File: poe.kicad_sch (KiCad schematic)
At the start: 59 parts, among them IC1 TPS2378DDA, J1 B2B-XH-A_LF__SN_, J6 SS-74800-144, U3 TPS2373-3RGW, U4 URB4805YMD-30WR3

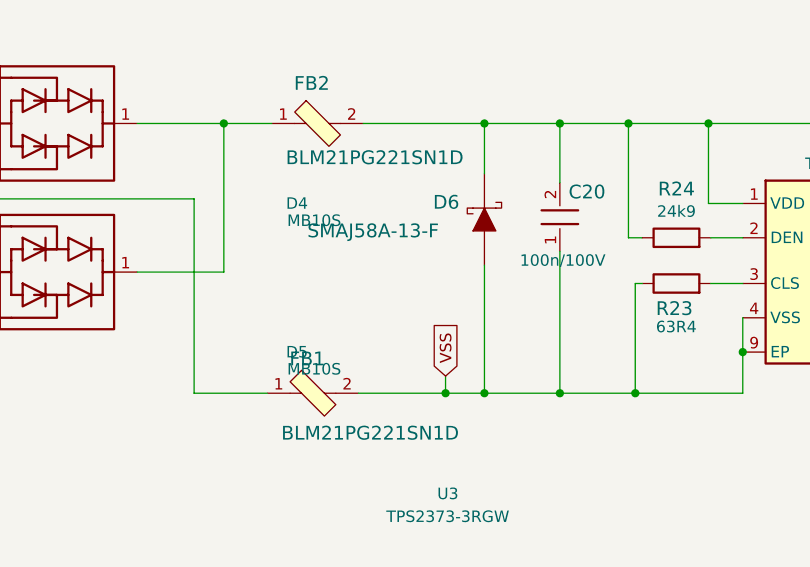
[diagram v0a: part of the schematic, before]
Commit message: Update D6 symbol and footprint
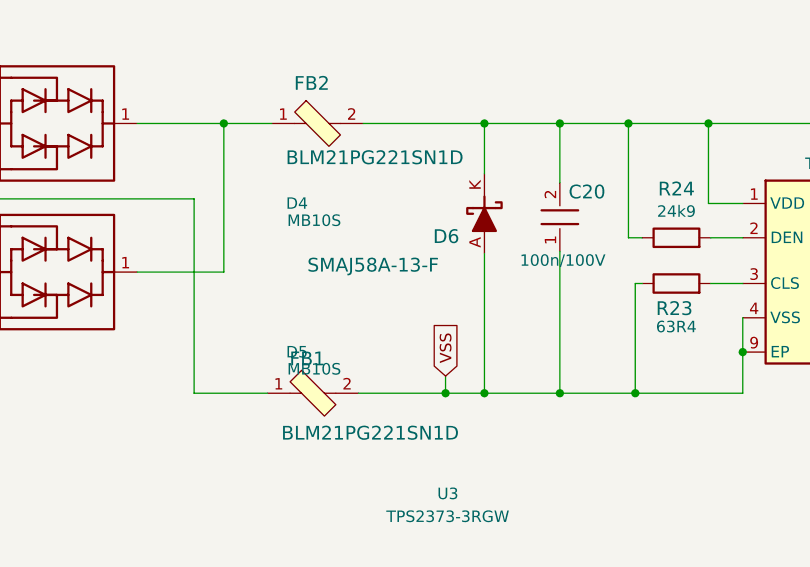
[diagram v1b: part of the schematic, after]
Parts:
- D6: footprint scalenode-cm4-baseboard-footprints:DO-214AC -> antmicro-footprints:DO-214AC; symbol scalenode-cm4-baseboard:SMAJ58A-13-F -> antmicroDiodesRectifiersSingle:SMAJ58A-13-F; Author (none) -> Antmicro; License (none) -> Apache-2.0
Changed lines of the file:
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@@
     (stroke (width 0) (type default) (color 0 0 0 0))
   )
-  (wire (pts (xy 109.982 165.608) (xy 109.982 179.832))
+  (wire (pts (xy 109.982 164.338) (xy 109.982 179.832))
     (stroke (width 0) (type default) (color 0 0 0 0))
   )
@@
     (pin "2")
   )
-  (symbol (lib_id "scalenode-cm4-baseboard:SMAJ58A-13-F") (at 109.982 160.528 90) (unit 1)
+  (symbol (lib_id "antmicroDiodesRectifiersSingle:SMAJ58A-13-F") (at 109.982 164.338 90) (unit 1)
     (in_bom yes) (on_board yes)
-    (property "Reference" "D6" (id 0) (at 104.267 158.623 90)
+    (property "Reference" "D6" (id 0) (at 104.267 162.433 90)
       (effects (font (size 1.524 1.524)) (justify right))
     )
-    (property "Value" "SMAJ58A-13-F" (id 1) (at 90.297 161.798 90)
+    (property "Value" "SMAJ58A-13-F" (id 1) (at 90.297 165.608 90)
       (effects (font (size 1.524 1.524)) (justify right))
     )
-    (property "Footprint" "scalenode-cm4-baseboard-footprints:DO-214AC" (id 2) (at 104.902 155.448 0)
-      (effects (font (size 1.524 1.524)) (justify left) hide)
+    (property "Footprint" "antmicro-footprints:DO-214AC" (id 2) (at 120.142 142.748 0)
+      (effects (font (size 1.27 1.27) (thickness 0.15)) (justify left bottom) hide)
     )
-    (property "Datasheet" "https://4donline.ihs.com/images/VipMasterIC/IC/DIOD/DIOD-S-A0001754755/DIOD-S-A0001754755-1.pdf?hkey=52A5661711E402568146F3353EA87419" (id 3) (at 102.362 155.448 0)
-      (effects (font (size 1.524 1.524)) (justify left) hide)
+    (property "Datasheet" "https://4donline.ihs.com/images/VipMasterIC/IC/DIOD/DIOD-S-A0001754755/DIOD-S-A0001754755-1.pdf?hkey=52A5661711E402568146F3353EA87419" (id 3) (at 122.682 142.748 0)
+      (effects (font (size 1.27 1.27) (thickness 0.15)) (justify left bottom) hide)
     )
-    (property "MPN" "SMAJ58A-13-F" (id 4) (at 97.282 155.448 0)
-      (effects (font (size 1.524 1.524)) (justify left) hide)
+    (property "MPN" "SMAJ58A-13-F" (id 4) (at 125.222 142.748 0)
+      (effects (font (size 1.27 1.27) (thickness 0.15)) (justify left bottom) hide)
     )
-    (property "Manufacturer" "Diodes Incorporated" (id 5) (at 82.042 155.448 0)
-      (effects (font (size 1.524 1.524)) (justify left) hide)
+    (property "Manufacturer" "Diodes Incorporated" (id 5) (at 127.762 142.748 0)
+      (effects (font (size 1.27 1.27) (thickness 0.15)) (justify left bottom) hide)
+    )
+    (property "Author" "Antmicro" (id 6) (at 130.302 142.748 0)
+      (effects (font (size 1.27 1.27) (thickness 0.15)) (justify left bottom) hide)
+    )
+    (property "License" "Apache-2.0" (id 7) (at 132.842 142.748 0)
+      (effects (font (size 1.27 1.27) (thickness 0.15)) (justify left bottom) hide)
     )
     (pin "A")

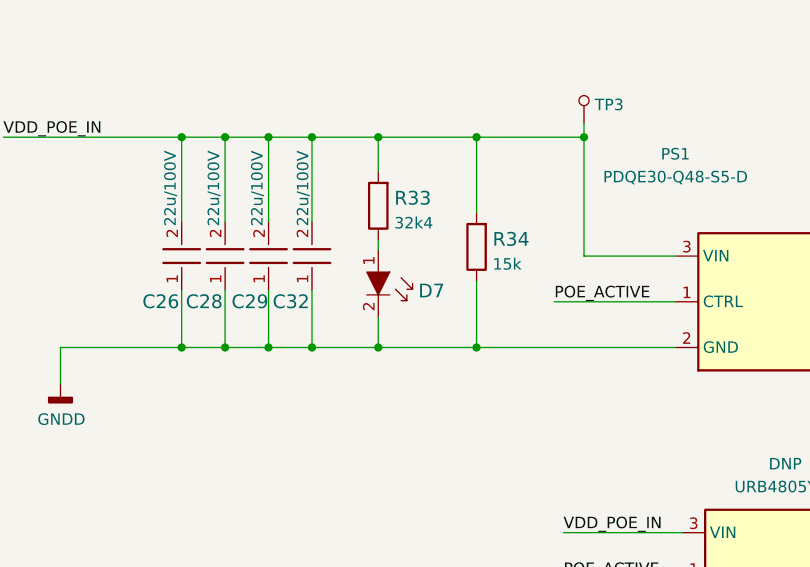
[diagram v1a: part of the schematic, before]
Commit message: Update D7 symbol and footprint
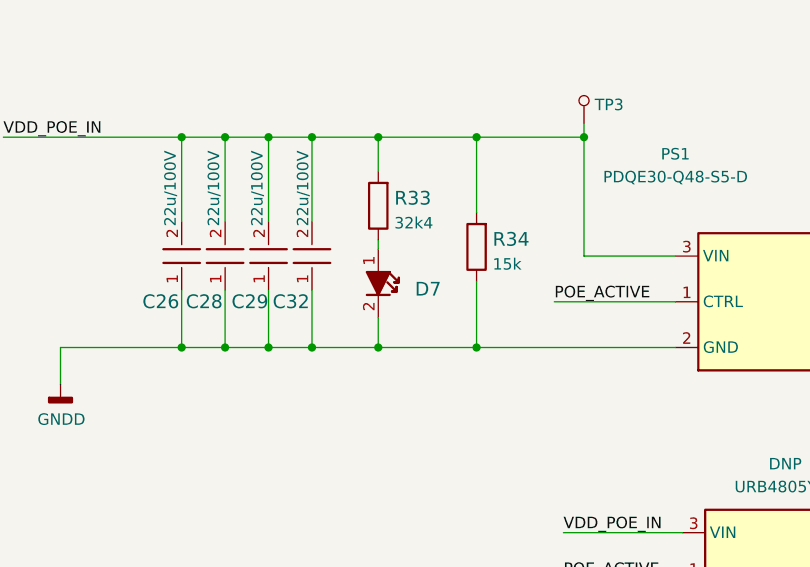
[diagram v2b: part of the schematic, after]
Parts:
- D7: footprint scalenode-cm4-baseboard-footprints:LED_0603 -> antmicro-footprints:LED_0603_1608Metric_G; symbol scalenode-cm4-baseboard:KP-1608CGCK -> antmicroLEDIndicationDiscrete:LED_G_0603_KP-1608CGCK; Author (none) -> Antmicro; License (none) -> Apache-2.0; Manufacturer KINGBRIGHT -> Kingbright
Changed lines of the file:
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@@
     (pin "1")
   )
-  (symbol (lib_id "scalenode-cm4-baseboard:KP-1608CGCK") (at 243.586 194.564 270) (unit 1)
+  (symbol (lib_id "antmicroLEDIndicationDiscrete:LED_G_0603_KP-1608CGCK") (at 243.586 189.484 270) (unit 1)
     (in_bom yes) (on_board yes) (fields_autoplaced)
-    (property "Reference" "D7" (id 0) (at 248.031 194.132 90)
+    (property "Reference" "D7" (id 0) (at 247.65 193.929 90)
       (effects (font (size 1.524 1.524)) (justify left))
     )
-    (property "Value" "KP-1608CGCK" (id 1) (at 248.1072 194.6402 90)
+    (property "Value" "KP-1608CGCK" (id 1) (at 248.1072 189.5602 90)
       (effects (font (size 1.524 1.524)) (justify left) hide)
     )
-    (property "Footprint" "scalenode-cm4-baseboard-footprints:LED_0603" (id 2) (at 248.666 199.644 0)
-      (effects (font (size 1.524 1.524)) (justify left) hide)
+    (property "Footprint" "antmicro-footprints:LED_0603_1608Metric_G" (id 2) (at 233.426 212.344 0)
+      (effects (font (size 1.27 1.27) (thickness 0.15)) (justify left bottom) hide)
     )
-    (property "Datasheet" "http://www.farnell.com/datasheets/2045956.pdf" (id 3) (at 251.206 199.644 0)
-      (effects (font (size 1.524 1.524)) (justify left) hide)
+    (property "Datasheet" "http://www.farnell.com/datasheets/2045956.pdf" (id 3) (at 230.886 212.344 0)
+      (effects (font (size 1.27 1.27) (thickness 0.15)) (justify left bottom) hide)
     )
-    (property "MPN" "KP-1608CGCK" (id 4) (at 256.286 199.644 0)
-      (effects (font (size 1.524 1.524)) (justify left) hide)
+    (property "MPN" "KP-1608CGCK" (id 4) (at 228.346 212.344 0)
+      (effects (font (size 1.27 1.27) (thickness 0.15)) (justify left bottom) hide)
     )
-    (property "Manufacturer" "KINGBRIGHT" (id 5) (at 259.334 199.898 0)
-      (effects (font (size 1.524 1.524)) (justify left) hide)
+    (property "Manufacturer" "Kingbright" (id 5) (at 225.806 212.344 0)
+      (effects (font (size 1.27 1.27) (thickness 0.15)) (justify left bottom) hide)
+    )
+    (property "Author" "Antmicro" (id 6) (at 223.266 212.344 0)
+      (effects (font (size 1.27 1.27) (thickness 0.15)) (justify left bottom) hide)
+    )
+    (property "License" "Apache-2.0" (id 7) (at 220.726 212.344 0)
+      (effects (font (size 1.27 1.27) (thickness 0.15)) (justify left bottom) hide)
     )
     (pin "1")

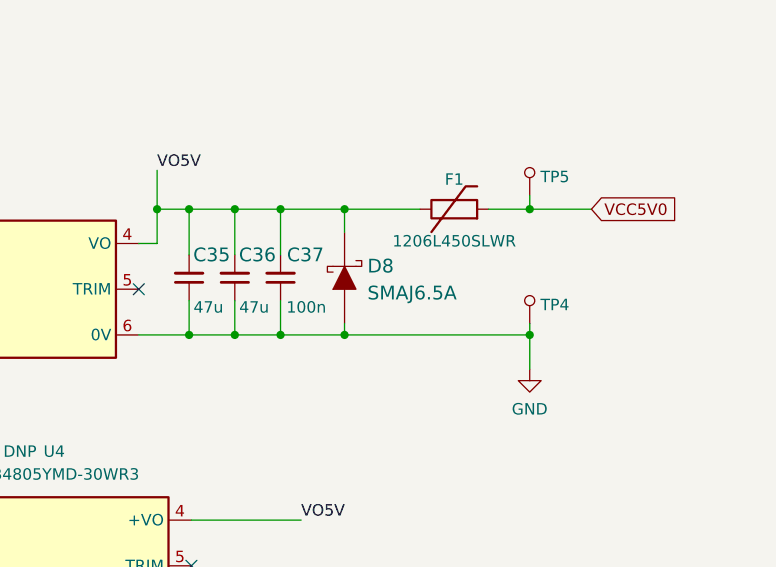
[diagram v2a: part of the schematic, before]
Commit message: Update D8 symbol and footprint
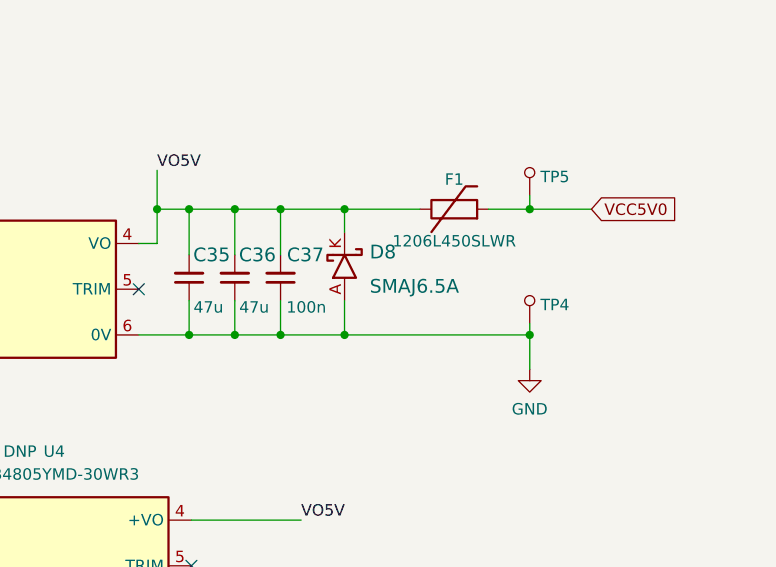
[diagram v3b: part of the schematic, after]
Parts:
- D8: footprint scalenode-cm4-baseboard-footprints:DO-214AC -> antmicro-footprints:DO-214AC; symbol scalenode-cm4-baseboard:SMAJ6.5A -> antmicroDiodesRectifiersSingle:SMAJ6.5A; Author (none) -> Antmicro; License (none) -> Apache-2.0; Manufacturer YAGEO -> Yaego
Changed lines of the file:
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@@
     (stroke (width 0) (type default) (color 0 0 0 0))
   )
-  (wire (pts (xy 324.866 199.136) (xy 324.866 200.406))
+  (wire (pts (xy 324.866 196.596) (xy 324.866 200.406))
     (stroke (width 0) (type default) (color 0 0 0 0))
   )
@@
     (pin "2")
   )
-  (symbol (lib_id "scalenode-cm4-baseboard:SMAJ6.5A") (at 324.866 194.056 90) (unit 1)
+  (symbol (lib_id "antmicroDiodesRectifiersSingle:SMAJ6.5A") (at 324.866 196.596 90) (unit 1)
     (in_bom yes) (on_board yes) (fields_autoplaced)
-    (property "Reference" "D8" (id 0) (at 327.406 192.7623 90)
+    (property "Reference" "D8" (id 0) (at 327.66 191.1985 90)
       (effects (font (size 1.524 1.524)) (justify right))
     )
-    (property "Value" "SMAJ6.5A" (id 1) (at 327.406 195.7557 90)
+    (property "Value" "SMAJ6.5A" (id 1) (at 327.66 195.0085 90)
       (effects (font (size 1.524 1.524)) (justify right))
     )
-    (property "Footprint" "scalenode-cm4-baseboard-footprints:DO-214AC" (id 2) (at 319.786 188.976 0)
-      (effects (font (size 1.524 1.524)) (justify left) hide)
+    (property "Footprint" "antmicro-footprints:DO-214AC" (id 2) (at 335.026 175.006 0)
+      (effects (font (size 1.27 1.27) (thickness 0.15)) (justify left bottom) hide)
     )
-    (property "Datasheet" "http://www.farnell.com/datasheets/2794252.pdf" (id 3) (at 317.246 188.976 0)
-      (effects (font (size 1.524 1.524)) (justify left) hide)
+    (property "Datasheet" "http://www.farnell.com/datasheets/2794252.pdf" (id 3) (at 337.566 175.006 0)
+      (effects (font (size 1.27 1.27) (thickness 0.15)) (justify left bottom) hide)
     )
-    (property "MPN" "SMAJ6.5A" (id 4) (at 312.166 188.976 0)
-      (effects (font (size 1.524 1.524)) (justify left) hide)
+    (property "MPN" "SMAJ6.5A" (id 4) (at 340.106 175.006 0)
+      (effects (font (size 1.27 1.27) (thickness 0.15)) (justify left bottom) hide)
     )
-    (property "Manufacturer" "YAGEO" (id 5) (at 296.926 188.976 0)
-      (effects (font (size 1.524 1.524)) (justify left) hide)
+    (property "Manufacturer" "Yaego" (id 5) (at 342.646 175.006 0)
+      (effects (font (size 1.27 1.27) (thickness 0.15)) (justify left bottom) hide)
+    )
+    (property "Author" "Antmicro" (id 6) (at 345.186 175.006 0)
+      (effects (font (size 1.27 1.27) (thickness 0.15)) (justify left bottom) hide)
+    )
+    (property "License" "Apache-2.0" (id 7) (at 347.726 175.006 0)
+      (effects (font (size 1.27 1.27) (thickness 0.15)) (justify left bottom) hide)
     )
     (pin "A")

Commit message: Updatae FB1, FB2 symbol and footprint
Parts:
- FB1, FB2: footprint scalenode-cm4-baseboard-footprints:0805-res -> antmicro-footprints:0805-res; symbol scalenode-cm4-baseboard:BLM21PG221SN1D -> antmicroFuses:BLM21PG221SN1D; Author (none) -> Antmicro; License (none) -> Apache-2.0
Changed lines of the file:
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@@
   (symbol (lib_id "antmicroTVSDiodes:MB10S") (at 71.374 149.86 0) (unit 1)
     (in_bom yes) (on_board yes)
-    (property "Reference" "D4" (id 0) (at 89.154 158.75 0))
-    (property "Value" "MB10S" (id 1) (at 91.059 160.655 0))
+    (property "Reference" "D4" (id 0) (at 71.628 151.638 0))
+    (property "Value" "MB10S" (id 1) (at 72.39 153.67 0))
     (property "Footprint" "antmicro-footprints:SOIC-4_4.2x5.0mm_P5.7mm" (id 2) (at 86.614 154.94 0)
       (effects (font (size 1.27 1.27) (thickness 0.15)) (justify left bottom) hide)
@@
     (pin "2")
   )
-  (symbol (lib_id "scalenode-cm4-baseboard:BLM21PG221SN1D") (at 90.932 179.832 0) (unit 1)
-    (in_bom yes) (on_board yes)
-    (property "Reference" "FB1" (id 0) (at 90.297 176.022 0)
+  (symbol (lib_id "antmicroFuses:BLM21PG221SN1D") (at 85.852 179.832 0) (unit 1)
+    (in_bom yes) (on_board yes)
+    (property "Reference" "FB1" (id 0) (at 85.217 176.022 0)
       (effects (font (size 1.524 1.524)))
     )
-    (property "Value" "BLM21PG221SN1D" (id 1) (at 97.282 184.277 0)
+    (property "Value" "BLM21PG221SN1D" (id 1) (at 92.202 183.642 0)
       (effects (font (size 1.524 1.524)))
     )
-    (property "Footprint" "scalenode-cm4-baseboard-footprints:0805-res" (id 2) (at 96.012 174.752 0)
-      (effects (font (size 1.524 1.524)) (justify left) hide)
-    )
-    (property "Datasheet" "" (id 3) (at 96.012 172.212 0)
-      (effects (font (size 1.524 1.524)) (justify left) hide)
-    )
-    (property "MPN" "BLM21PG221SN1D" (id 4) (at 96.012 167.132 0)
-      (effects (font (size 1.524 1.524)) (justify left) hide)
-    )
-    (property "Manufacturer" "Murata Electronics North America" (id 5) (at 96.012 151.892 0)
-      (effects (font (size 1.524 1.524)) (justify left) hide)
+    (property "Footprint" "antmicro-footprints:0805-res" (id 2) (at 111.252 187.452 0)
+      (effects (font (size 1.27 1.27) (thickness 0.15)) (justify left bottom) hide)
+    )
+    (property "Datasheet" "" (id 3) (at 111.252 189.992 0)
+      (effects (font (size 1.27 1.27) (thickness 0.15)) (justify left bottom) hide)
+    )
+    (property "MPN" "BLM21PG221SN1D" (id 4) (at 111.252 192.532 0)
+      (effects (font (size 1.27 1.27) (thickness 0.15)) (justify left bottom) hide)
+    )
+    (property "Manufacturer" "Murata Electronics North America" (id 5) (at 111.252 195.072 0)
+      (effects (font (size 1.27 1.27) (thickness 0.15)) (justify left bottom) hide)
+    )
+    (property "Author" "Antmicro" (id 6) (at 111.252 197.612 0)
+      (effects (font (size 1.27 1.27) (thickness 0.15)) (justify left bottom) hide)
+    )
+    (property "License" "Apache-2.0" (id 7) (at 111.252 200.152 0)
+      (effects (font (size 1.27 1.27) (thickness 0.15)) (justify left bottom) hide)
     )
     (pin "1")
@@
     (pin "2")
   )
-  (symbol (lib_id "scalenode-cm4-baseboard:BLM21PG221SN1D") (at 91.44 149.86 0) (unit 1)
-    (in_bom yes) (on_board yes)
-    (property "Reference" "FB2" (id 0) (at 90.805 145.415 0)
+  (symbol (lib_id "antmicroFuses:BLM21PG221SN1D") (at 86.36 149.86 0) (unit 1)
+    (in_bom yes) (on_board yes)
+    (property "Reference" "FB2" (id 0) (at 85.725 145.415 0)
       (effects (font (size 1.524 1.524)))
     )
-    (property "Value" "BLM21PG221SN1D" (id 1) (at 97.79 153.67 0)
+    (property "Value" "BLM21PG221SN1D" (id 1) (at 92.71 153.67 0)
       (effects (font (size 1.524 1.524)))
     )
-    (property "Footprint" "scalenode-cm4-baseboard-footprints:0805-res" (id 2) (at 96.52 144.78 0)
-      (effects (font (size 1.524 1.524)) (justify left) hide)
-    )
-    (property "Datasheet" "" (id 3) (at 96.52 142.24 0)
-      (effects (font (size 1.524 1.524)) (justify left) hide)
-    )
-    (property "MPN" "BLM21PG221SN1D" (id 4) (at 96.52 137.16 0)
-      (effects (font (size 1.524 1.524)) (justify left) hide)
-    )
-    (property "Manufacturer" "Murata Electronics North America" (id 5) (at 96.52 121.92 0)
-      (effects (font (size 1.524 1.524)) (justify left) hide)
+    (property "Footprint" "antmicro-footprints:0805-res" (id 2) (at 111.76 157.48 0)
+      (effects (font (size 1.27 1.27) (thickness 0.15)) (justify left bottom) hide)
+    )
+    (property "Datasheet" "" (id 3) (at 111.76 160.02 0)
+      (effects (font (size 1.27 1.27) (thickness 0.15)) (justify left bottom) hide)
+    )
+    (property "MPN" "BLM21PG221SN1D" (id 4) (at 111.76 162.56 0)
+      (effects (font (size 1.27 1.27) (thickness 0.15)) (justify left bottom) hide)
+    )
+    (property "Manufacturer" "Murata Electronics North America" (id 5) (at 111.76 165.1 0)
+      (effects (font (size 1.27 1.27) (thickness 0.15)) (justify left bottom) hide)
+    )
+    (property "Author" "Antmicro" (id 6) (at 111.76 167.64 0)
+      (effects (font (size 1.27 1.27) (thickness 0.15)) (justify left bottom) hide)
+    )
+    (property "License" "Apache-2.0" (id 7) (at 111.76 170.18 0)
+      (effects (font (size 1.27 1.27) (thickness 0.15)) (justify left bottom) hide)
     )
     (pin "1")
@@
   (symbol (lib_id "antmicroTVSDiodes:MB10S") (at 71.374 166.37 0) (unit 1)
     (in_bom yes) (on_board yes)
-    (property "Reference" "D5" (id 0) (at 89.154 175.26 0))
-    (property "Value" "MB10S" (id 1) (at 91.059 177.165 0))
+    (property "Reference" "D5" (id 0) (at 71.882 167.894 0))
+    (property "Value" "MB10S" (id 1) (at 72.39 169.926 0))
     (property "Footprint" "antmicro-footprints:SOIC-4_4.2x5.0mm_P5.7mm" (id 2) (at 86.614 171.45 0)
       (effects (font (size 1.27 1.27) (thickness 0.15)) (justify left bottom) hide)
